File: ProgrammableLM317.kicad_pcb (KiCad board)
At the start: 2 copper layers, 49.5 x 49.5 mm, 28 parts, among them IC1 ATTINY85-P, K1 CONN_3, P1 CONN_2, P2 CONN_2, U1 LM317, U2 LM358, U3 MCP4801, U4 7805

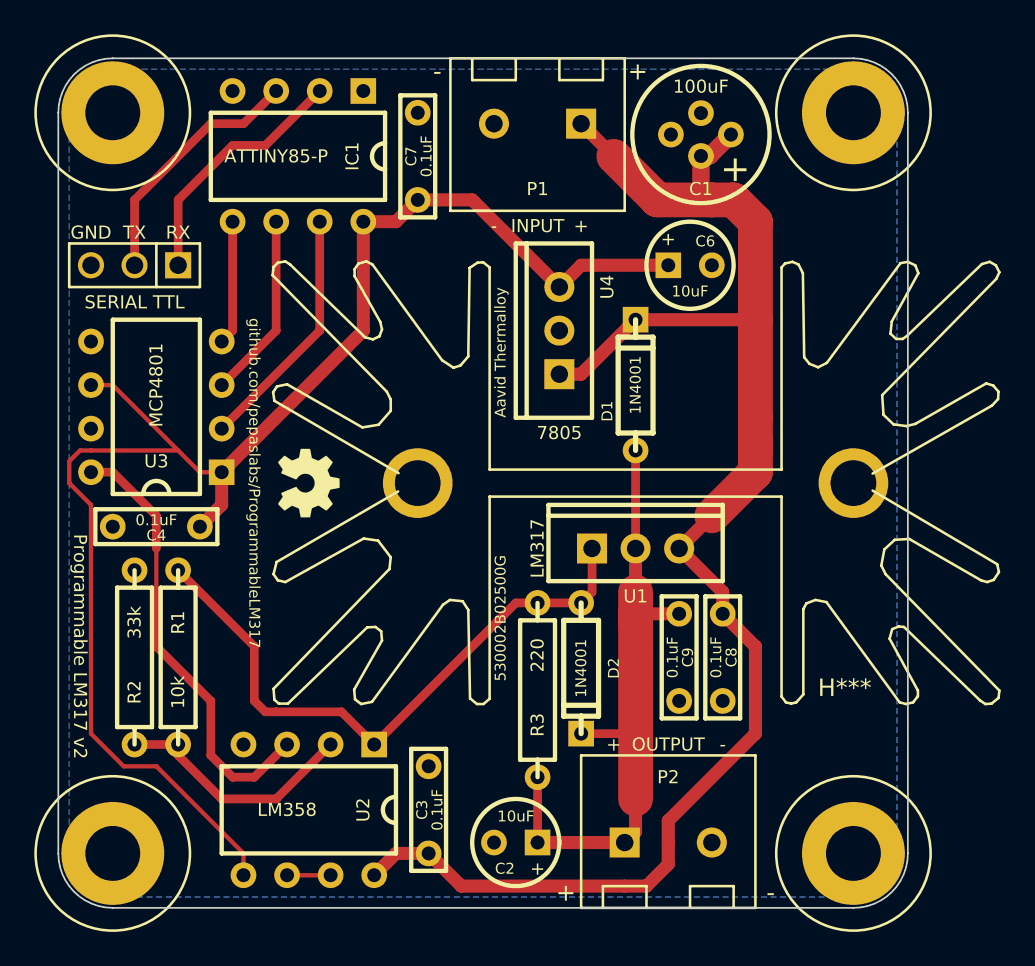
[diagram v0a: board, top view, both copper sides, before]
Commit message: adding connector to supply negative rail to op amp.
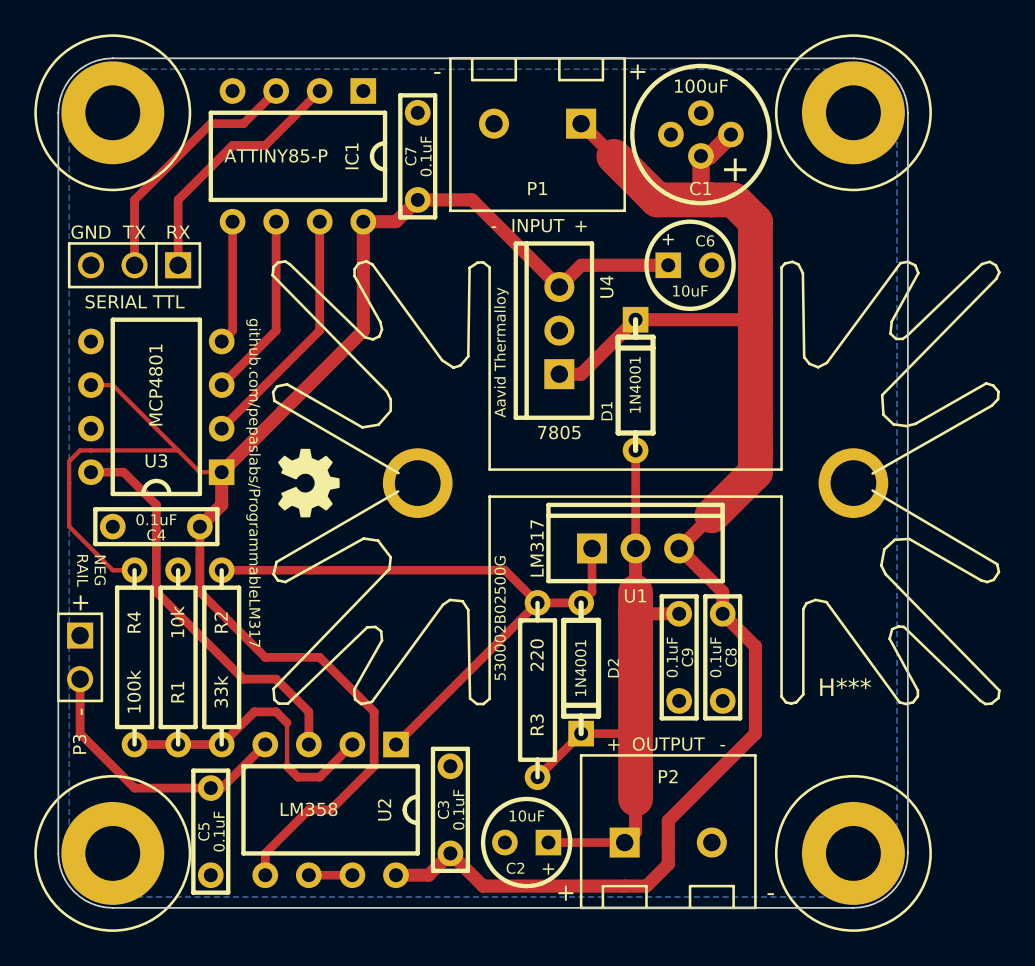
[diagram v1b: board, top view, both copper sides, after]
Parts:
- added C5: 0.1uF, CERCAP_2_059A, F.Cu at (130.8, 168.3)
- added P3: CONN_2, PIN_ARRAY_2X1, F.Cu at (123.2, 158.1)
- added R4: 100k, R_AXIAL_0W25_059A, F.Cu at (126.4, 153.0)
- moved R2 11.4 mm to (131.4, 153.0), turned to 270 degrees
- moved R1 10.2 mm to (128.9, 163.2), turned to 90 degrees
- moved C3 1.27 mm to (144.8, 167.0)
- moved U2 1.27 mm to (141.6, 163.2)
- moved C2 0.63 mm to (150.5, 168.9)
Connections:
- D2 pad 1: N-0000016 (its old number) -> N-0000014
- R1 pad 1: N-0000016 (its old number) -> N-0000013
- R1 pad 2: N-0000018 -> GND
- R2 pad 1: N-0000018 -> N-0000014
- R2 pad 2: GND -> N-0000013
- R3 pad 2: N-0000016 (its old number) -> N-0000014
- U1 pad 1: N-0000016 (its old number) -> N-0000014
- U2 pad 1: N-0000016 (its old number) -> N-0000014
- U2 pad 2: N-0000018 -> N-0000013
- U2 pad 4: GND -> Vee
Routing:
- net N-0000014: track 0.00 -> 36.9 mm
- net N-0000016 (its old number): track 36.4 -> 0.00 mm
- net N-0000013: track 0.00 -> 17.3 mm
- net Vee: track 0.00 -> 16.3 mm
- net N-0000018: track 14.4 -> 0.00 mm
- net 5V: track 88.5 -> 97.4 mm
- net N-0000019: track 25.9 -> 23.4 mm
- net Vcc: track 92.6 -> 91.3 mm
- net Vout: track 37.7 -> 36.9 mm
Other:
- board text added: "NEG RAIL"
- board text removed: "Programmable LM317 v2"

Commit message: using multi-footprint for input and output connectors.
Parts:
- moved U4 7.24 mm to (158.1, 139.7), turned to 180 degrees
- moved D1 3.86 mm to (159.4, 145.4), turned to 180 degrees
- moved C6 0.63 mm to (157.5, 134.6)
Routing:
- net 5V: track 97.4 -> 100.5 mm
- net Vcc: track 91.3 -> 94.4 mm
- net Vout: track 36.9 -> 39.1 mm

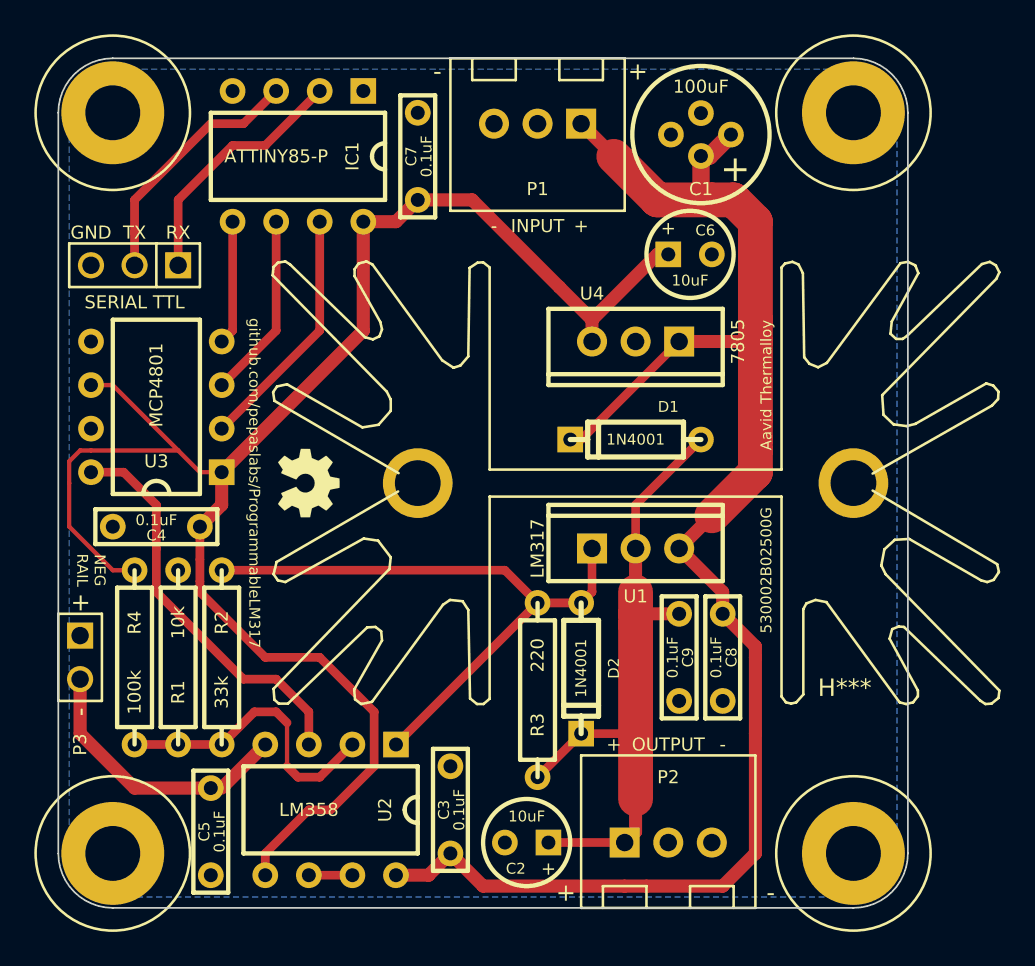
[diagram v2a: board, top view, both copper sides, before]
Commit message: using multi-footprints for ceramic bypass capacitors
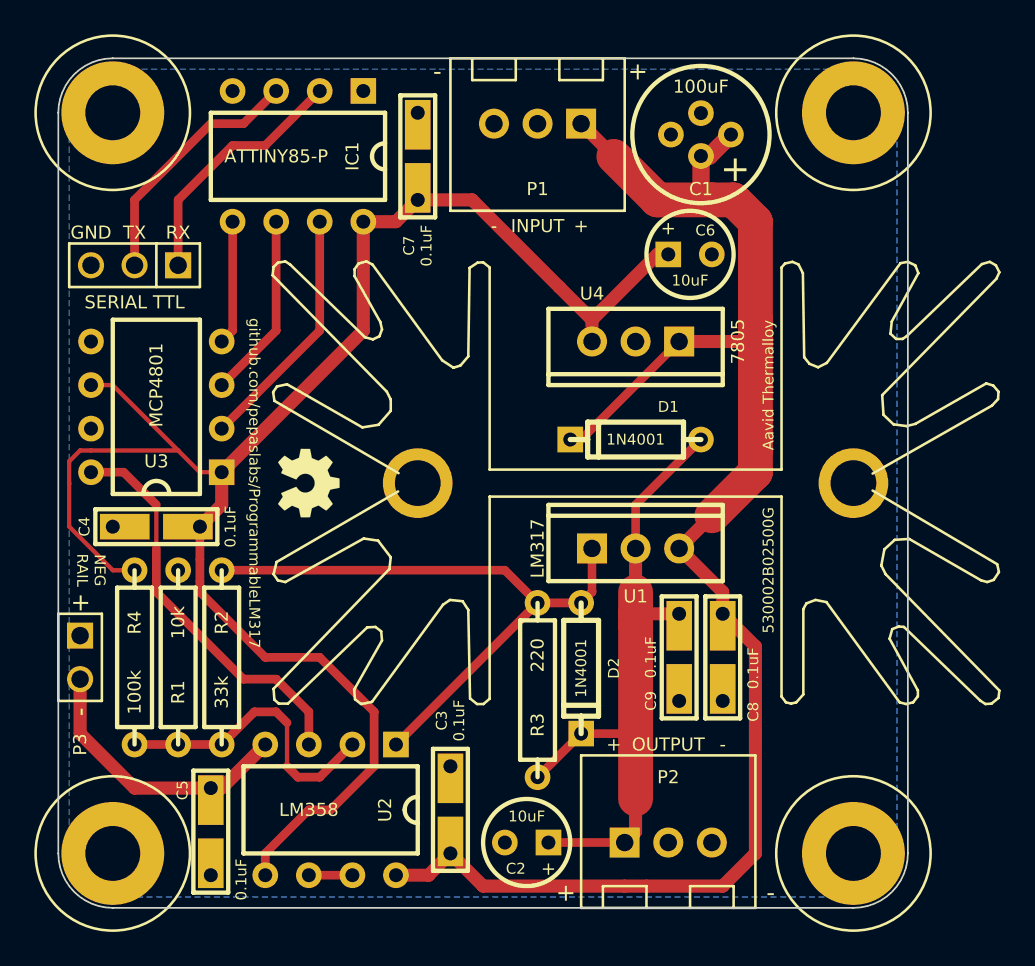
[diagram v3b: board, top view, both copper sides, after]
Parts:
- C3, C4, C5, C7, C8, C9: footprint CERCAP_2_059A -> CERCAP_2_059B_0805
